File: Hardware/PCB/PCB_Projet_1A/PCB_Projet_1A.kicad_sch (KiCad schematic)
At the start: 36 parts, among them J1 Conn_01x02, J10 Conn_ST_STDC14, J11 Conn_01x03, J12 Conn_01x03, J2 Conn_01x02, J3 Conn_01x02, J4 BU33SD5WG-TR, J5 R-78B5.0-2.0, J6 Conn_01x04, J7 Conn_01x04, J8 Conn_01x04, J9 Conn_01x04, U1 STM32L552CCTx

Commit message: modification schematique
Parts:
- removed C1: 4u7, Capacitor_SMD:C_0805_2012Metric, symbol Device:C
- removed C13, C14: 1uF, Capacitor_SMD:C_0603_1608Metric_Pad1.08x0.95mm_HandSolder, symbol Device:C
- removed C2, C6: 100n, Capacitor_SMD:C_0402_1005Metric, symbol Device:C
- removed C5, C7: 10n, Capacitor_SMD:C_0402_1005Metric, symbol Device:C
- removed C8: 1u, Capacitor_SMD:C_0402_1005Metric, symbol Device:C
- removed J3: Conn_01x02, Connector_JST:JST_XH_S2B-XH-A-1_1x02_P2.50mm_Horizontal, symbol Connector_Generic:Conn_01x02
- removed J4: BU33SD5WG-TR, BU33SD5WG-TR:SOT95P280X125-5N, symbol BU33SD5WG-TR:BU33SD5WG-TR
- removed J5: R-78B5.0-2.0, Converter_DCDC:Converter_DCDC_RECOM_R-78B-2.0_THT, symbol Regulator_Switching:R-78B5.0-2.0
- removed L1: 39n, Inductor_SMD:L_0603_1608Metric, symbol Device:L
- removed Switch1: 430471025826, boutonSMD_wurth430471025826:430471025826, symbol boutonSMD_wurth430471025826:430471025826
- removed TP1, TP2: TestPoint, TestPoint:TestPoint_Pad_D2.0mm, symbol Connector:TestPoint
- removed U1: STM32L552CCTx, Package_QFP:LQFP-48_7x7mm_P0.5mm, symbol MCU_ST_STM32L5:STM32L552CCTx
- added D1: LED, symbol Device:LED
- added R1: 470, symbol Device:R
- added SW1: SW_Push, symbol Switch:SW_Push
- added U2: HC-05, HC-05:XCVR_HC-05, symbol HC-05:HC-05
- C3, C4: footprint Capacitor_SMD:C_0402_1005Metric -> (none)
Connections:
- net +3.3V: now also U2.12 (3.3_VCC); no longer C3.1
- net GND: now also C3.1, R1.1, U2.13 (GND), U2.21 (GND), U2.22 (GND); no longer C3.2
- new net: SW1.2, U2.11 (~{RESETB})
- new net: D1.2 (A), U2.24 (PIO[1])
- new net: D1.1 (K), R1.2
- new net: C3.2, SW1.1
- new net UART4_RX: U2.2 (UART-RX)
- new net UART4_TX: U2.1 (UART-TX)
- no-connect marks 20 -> 28
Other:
- added sheet MCU, Alimentation et Régulateurs (MCU_REGU.kicad_sch)
- note added: "HC-05"
- note removed: "Alimentation des piles et régulateurs de tension"
- note removed: "MCU"
- moved on the sheet: C10, C11, C12, C9, Driver1, H1, H2, H3, H4, J1, J10, J11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

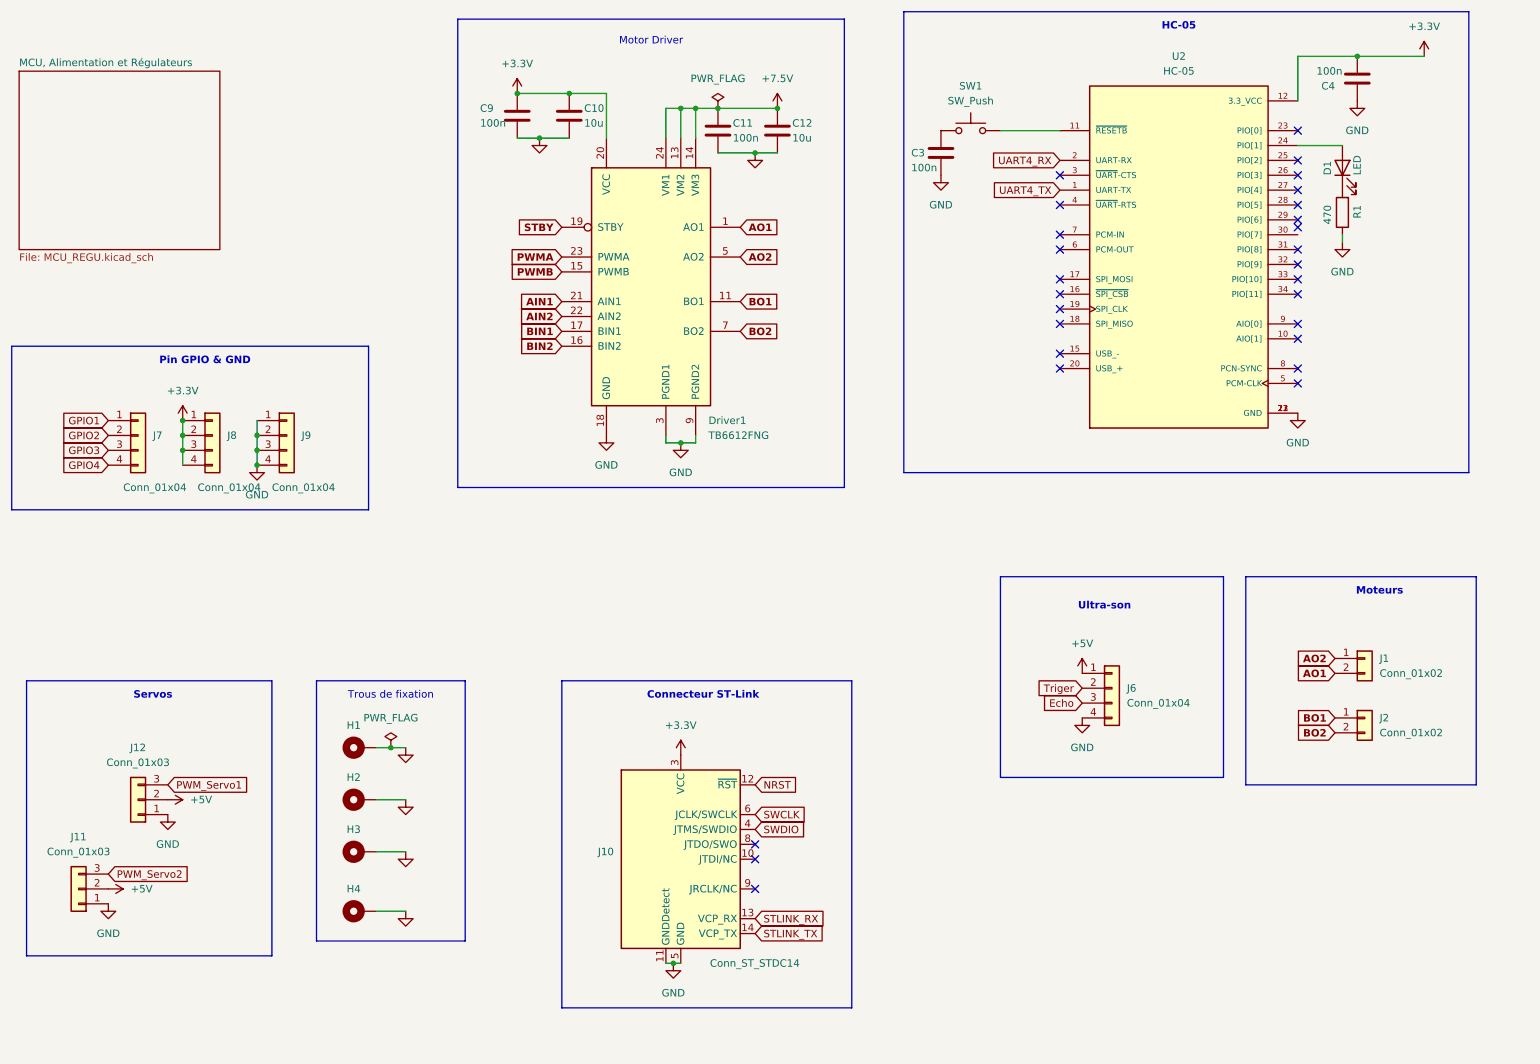
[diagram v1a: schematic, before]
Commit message: finalisation schématique PCB
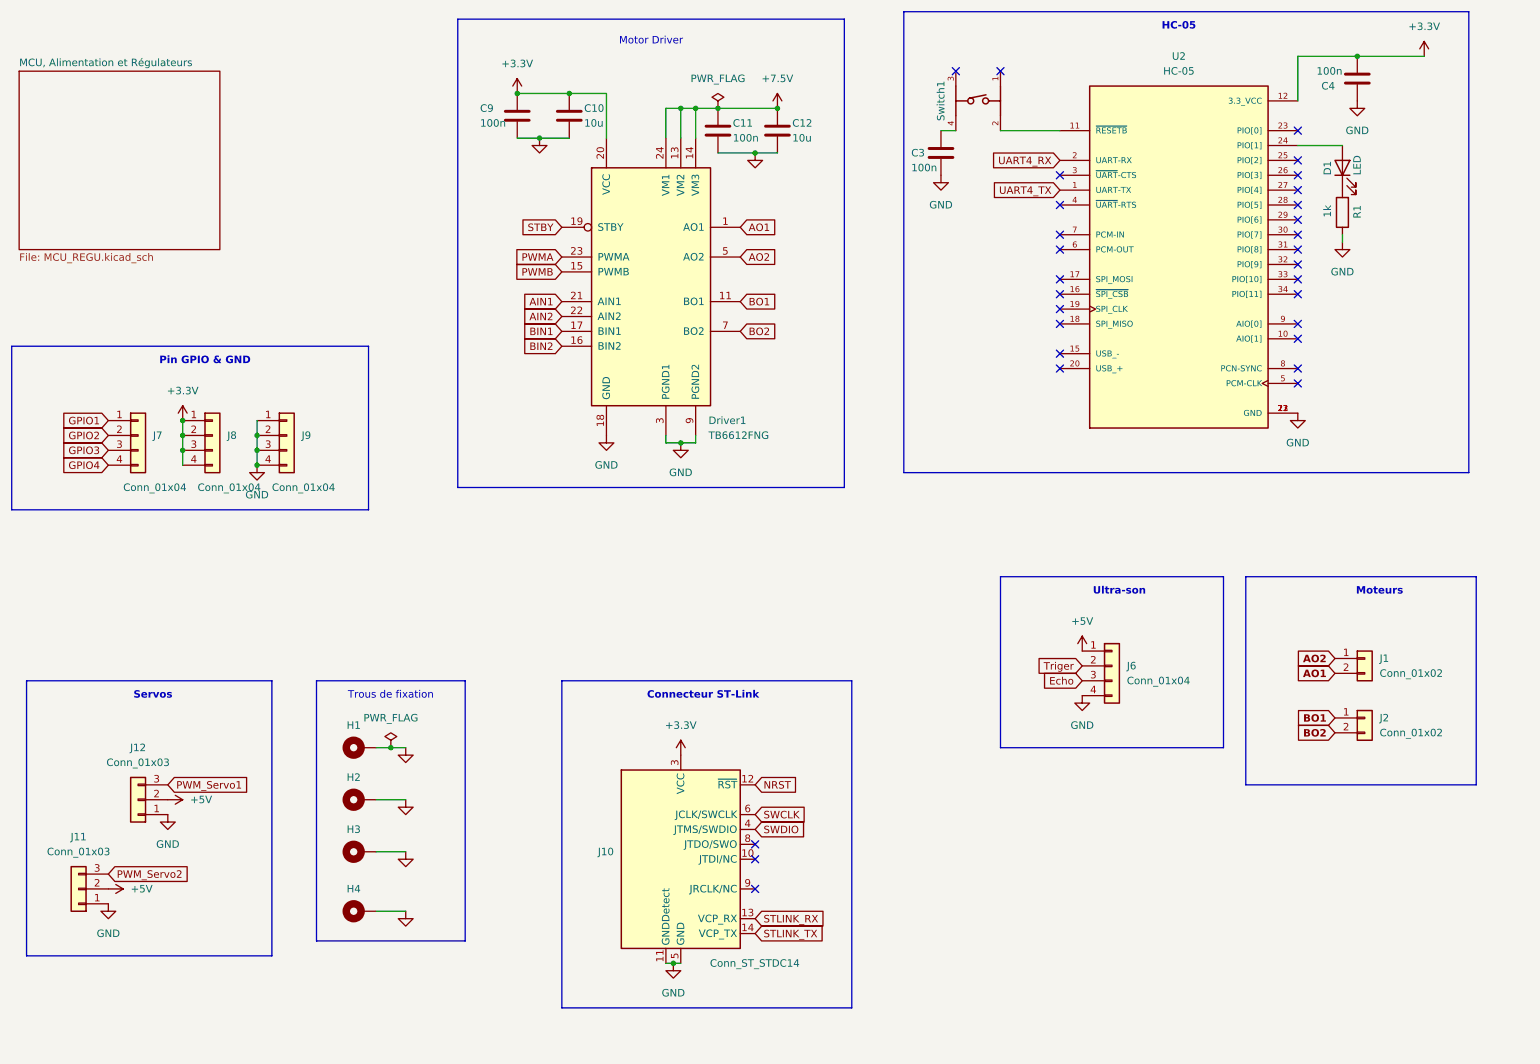
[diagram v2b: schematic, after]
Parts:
- removed SW1: SW_Push, symbol Switch:SW_Push
- added Switch1: 430471025826, boutonSMD_wurth430471025826:430471025826, symbol boutonSMD_wurth430471025826:430471025826
- C3, C4: footprint (none) -> Capacitor_SMD:C_0402_1005Metric
- D1: footprint (none) -> LED_SMD:LED_0603_1608Metric_Pad1.05x0.95mm_HandSolder
- R1: value 470 -> 1k; footprint (none) -> Resistor_SMD:R_0603_1608Metric_Pad0.98x0.95mm_HandSolder
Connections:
- net at U2.11 (~{RESETB}): now also Switch1.2
- net at C3.2: now also Switch1.4
- no-connect marks 28 -> 30
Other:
- moved on the sheet: J6

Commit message: Avancement sur le PCB editor
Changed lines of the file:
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@@
 	(wire
 		(pts
-			(xy 86.36 168.91) (xy 91.44 168.91)
-		)
-		(stroke
-			(width 0)
-			(type default)
-		)
-	)
-	(wire
-		(pts
 			(xy 86.36 140.97) (xy 88.9 140.97)
 		)
@@
 		)
 	)
+	(wire
+		(pts
+			(xy 87.63 166.37) (xy 92.71 166.37)
+		)
+		(stroke
+			(width 0)
+			(type default)
+		)
+	)
 	(rectangle
 		(start 176.53 15.24)
@@
 	)
 	(symbol
-		(lib_name "MountingHole_Pad_2")
-		(lib_id "Mechanical:MountingHole_Pad")
-		(at 83.82 168.91 90)
-		(unit 1)
-		(exclude_from_sim yes)
-		(in_bom no)
-		(on_board yes)
-		(dnp no)
-		(fields_autoplaced yes)
-		(property "Reference" "H4"
-			(at 82.55 165.1 90)
-			(effects
-				(font
-					(size 1.27 1.27)
-				)
-			)
-		)
-		(property "Value" "MountingHole_Pad"
-			(at 83.8199 166.37 0)
-			(effects
-				(font
-					(size 1.27 1.27)
-				)
-				(justify left)
-				(hide yes)
-			)
-		)
-		(property "Footprint" "MountingHole:MountingHole_2.7mm_M2.5_Pad"
-			(at 83.82 168.91 0)
-			(effects
-				(font
-					(size 1.27 1.27)
-				)
-				(hide yes)
-			)
-		)
-		(property "Datasheet" "~"
-			(at 83.82 168.91 0)
-			(effects
-				(font
-					(size 1.27 1.27)
-				)
-				(hide yes)
-			)
-		)
-		(property "Description" "Mounting Hole with connection"
-			(at 83.82 168.91 0)
-			(effects
-				(font
-					(size 1.27 1.27)
-				)
-				(hide yes)
-			)
-		)
-		(pin "1"
-		)
-		(instances
-			(project "PCB_Projet_1A"
-				(path "/f089084e-de1a-4032-a3c6-cf342d345630"
-					(reference "H4")
-					(unit 1)
-				)
-			)
-		)
-	)
-	(symbol
 		(lib_id "Device:C")
 		(at 119.38 33.02 0)
@@
 	)
 	(symbol
+		(lib_name "MountingHole_Pad_2")
+		(lib_id "Mechanical:MountingHole_Pad")
+		(at 85.09 166.37 90)
+		(unit 1)
+		(exclude_from_sim yes)
+		(in_bom no)
+		(on_board yes)
+		(dnp no)
+		(fields_autoplaced yes)
+		(property "Reference" "H4"
+			(at 83.82 162.56 90)
+			(effects
+				(font
+					(size 1.27 1.27)
+				)
+			)
+		)
+		(property "Value" "MountingHole_Pad"
+			(at 85.0899 163.83 0)
+			(effects
+				(font
+					(size 1.27 1.27)
+				)
+				(justify left)
+				(hide yes)
+			)
+		)
+		(property "Footprint" "MountingHole:MountingHole_2.7mm_M2.5_Pad"
+			(at 85.09 166.37 0)
+			(effects
+				(font
+					(size 1.27 1.27)
+				)
+				(hide yes)
+			)
+		)
+		(property "Datasheet" "~"
+			(at 85.09 166.37 0)
+			(effects
+				(font
+					(size 1.27 1.27)
+				)
+				(hide yes)
+			)
+		)
+		(property "Description" "Mounting Hole with connection"
+			(at 85.09 166.37 0)
+			(effects
+				(font
+					(size 1.27 1.27)
+				)
+				(hide yes)
+			)
+		)
+		(pin "1"
+		)
+		(instances
+			(project "PCB_Projet_1A"
+				(path "/f089084e-de1a-4032-a3c6-cf342d345630"
+					(reference "H4")
+					(unit 1)
+				)
+			)
+		)
+	)
+	(symbol
 		(lib_id "Connector_Generic:Conn_01x04")
 		(at 58.42 87.63 0)
@@
 	(symbol
 		(lib_id "power:GND")
-		(at 91.44 168.91 0)
-		(unit 1)
-		(exclude_from_sim no)
-		(in_bom yes)
-		(on_board yes)
-		(dnp no)
-		(fields_autoplaced yes)
-		(property "Reference" "#PWR031"
-			(at 91.44 175.26 0)
-			(effects
-				(font
-					(size 1.27 1.27)
-				)
-				(hide yes)
-			)
-		)
-		(property "Value" "GND"
-			(at 91.44 173.99 0)
-			(effects
-				(font
-					(size 1.27 1.27)
-				)
-				(hide yes)
-			)
-		)
-		(property "Footprint" ""
-			(at 91.44 168.91 0)
-			(effects
-				(font
-					(size 1.27 1.27)
-				)
-				(hide yes)
-			)
-		)
-		(property "Datasheet" ""
-			(at 91.44 168.91 0)
-			(effects
-				(font
-					(size 1.27 1.27)
-				)
-				(hide yes)
-			)
-		)
-		(property "Description" "Power symbol creates a global label with name \"GND\" , ground"
-			(at 91.44 168.91 0)
-			(effects
-				(font
-					(size 1.27 1.27)
-				)
-				(hide yes)
-			)
-		)
-		(pin "1"
-		)
-		(instances
-			(project "PCB_Projet_1A"
-				(path "/f089084e-de1a-4032-a3c6-cf342d345630"
-					(reference "#PWR031")
-					(unit 1)
-				)
-			)
-		)
-	)
-	(symbol
-		(lib_id "power:GND")
 		(at 40.64 167.64 0)
 		(unit 1)
@@
 					(unit 1)
 				)
+			)
+		)
+	)
+	(symbol
+		(lib_id "power:GND")
+		(at 92.71 166.37 0)
+		(unit 1)
+		(exclude_from_sim no)
+		(in_bom yes)
+		(on_board yes)
+		(dnp no)
+		(fields_autoplaced yes)
+		(property "Reference" "#PWR019"
+			(at 92.71 172.72 0)
+			(effects
+				(font
+					(size 1.27 1.27)
+				)
+				(hide yes)
+			)
+		)
+		(property "Value" "GND"
+			(at 92.71 171.45 0)
+			(effects
+				(font
+					(size 1.27 1.27)
+				)
+				(hide yes)
+			)
+		)
+		(property "Footprint" ""
+			(at 92.71 166.37 0)
+			(effects
+				(font
+					(size 1.27 1.27)
+				)
+				(hide yes)
+			)
+		)
+		(property "Datasheet" ""
+			(at 92.71 166.37 0)
+			(effects
+				(font
+					(size 1.27 1.27)
+				)
+				(hide yes)
+			)
+		)
+		(property "Description" "Power symbol creates a global label with name \"GND\" , ground"
+			(at 92.71 166.37 0)
+			(effects
+				(font
+					(size 1.27 1.27)
+				)
+				(hide yes)
+			)
+		)
+		(pin "1"
+		)
+		(instances
+			(project "PCB_Projet_1A"
+				(path "/f089084e-de1a-4032-a3c6-cf342d345630"
+					(reference "#PWR019")
+					(unit 1)
+				)

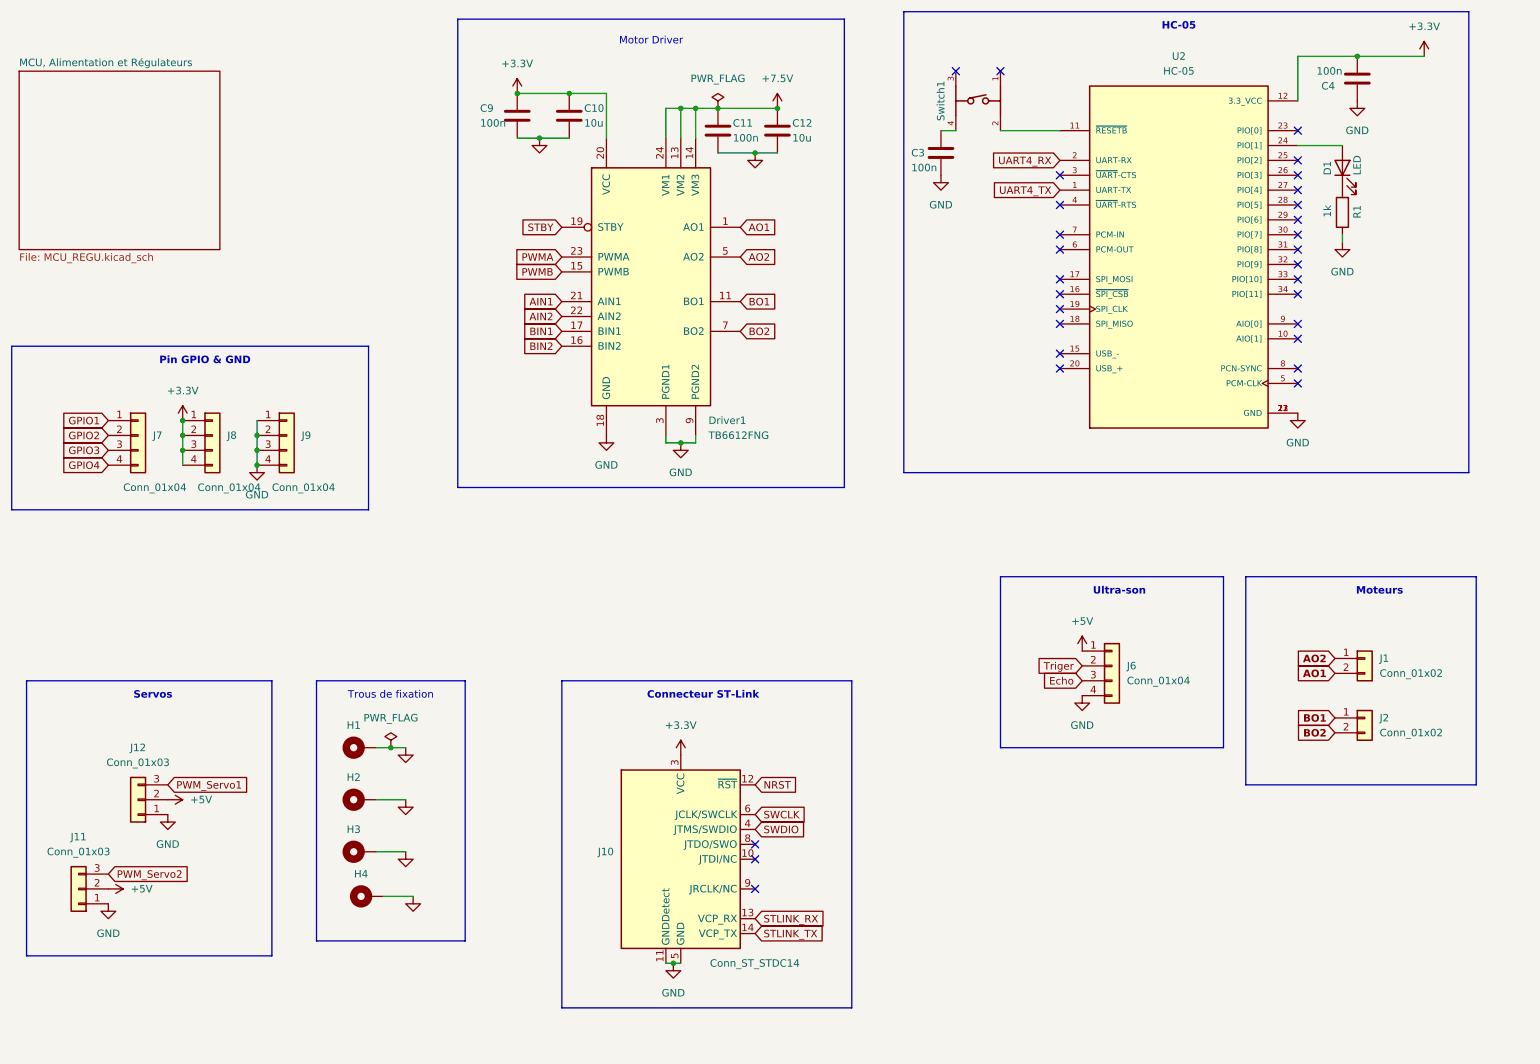
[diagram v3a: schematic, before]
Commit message: Finalisation du PCB et ajout du README dans le répertoire PCB
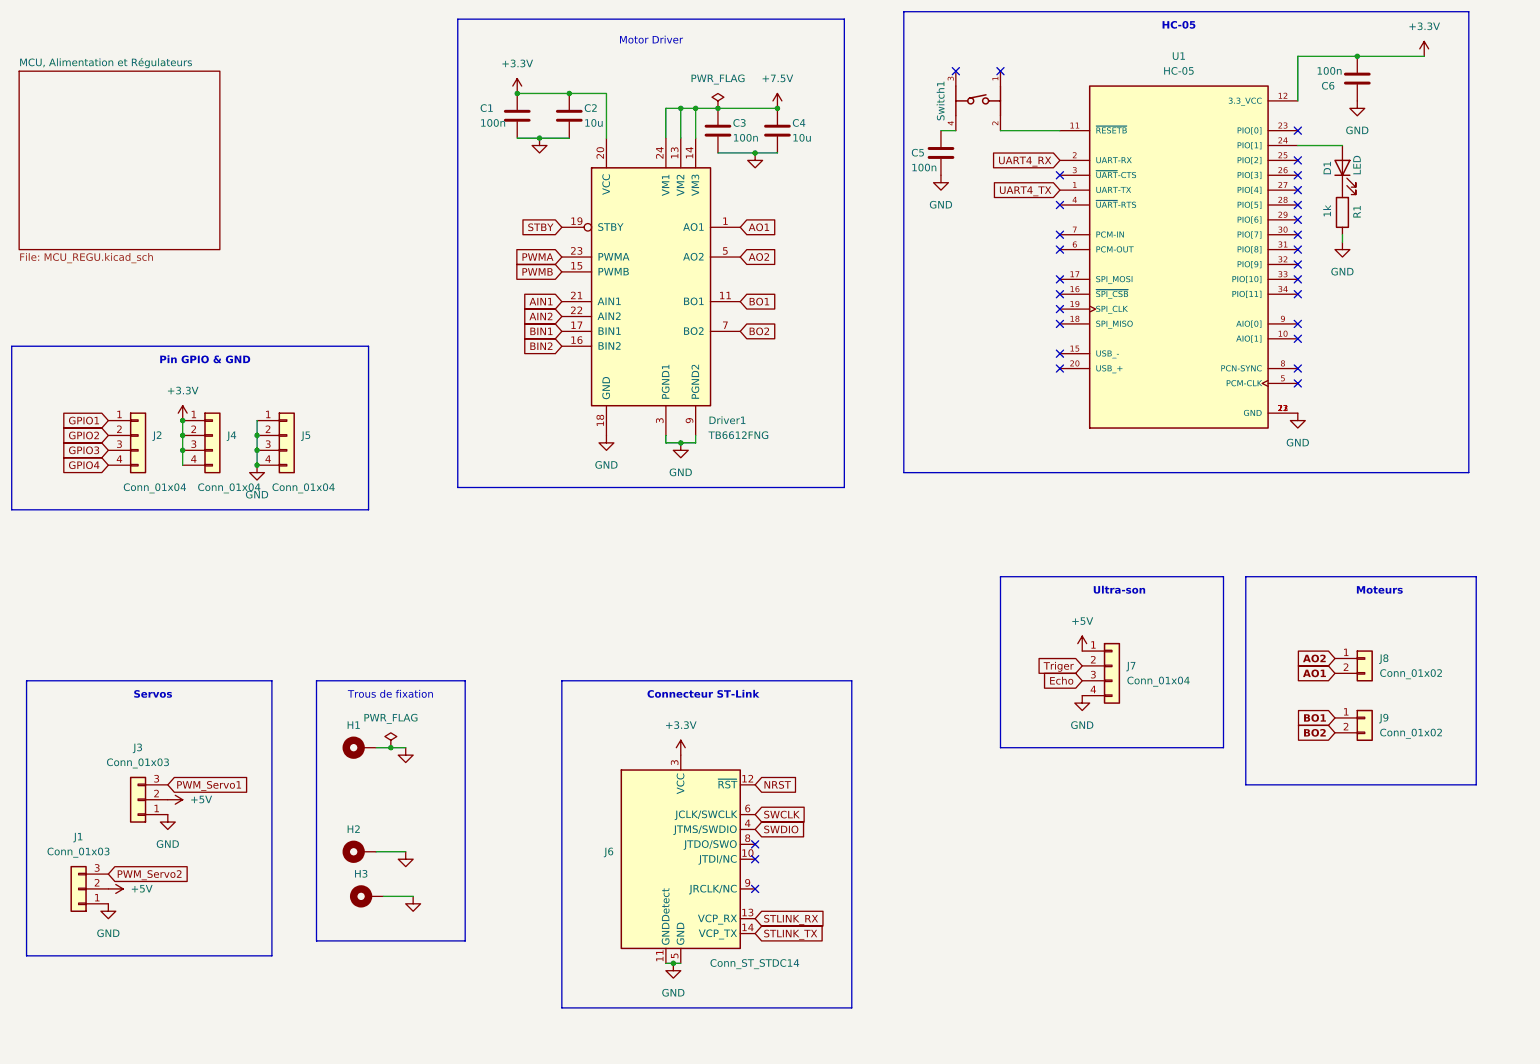
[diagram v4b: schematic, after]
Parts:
- removed H2: MountingHole_Pad, MountingHole:MountingHole_2.7mm_M2.5_Pad, symbol Mechanical:MountingHole_Pad
- renumbered C9 to C1, C10 to C2, C11 to C3, C12 to C4, C3 to C5, C4 to C6, H3 to H2, H4 to H3, J11 to J1, J7 to J2, J12 to J3, J8 to J4, J9 to J5, J10 to J6, J6 to J7, J1 to J8, J2 to J9, U2 to U1
